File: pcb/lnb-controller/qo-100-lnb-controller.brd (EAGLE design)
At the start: 70 x 100 mm, 168 parts, among them CON1 3P-SH-SIDE, CON2 2EDG-2P-5MM, U1 EFM32PG1B100F256GM32, U10 ADP7142AUJZ-3.3, U3 DSB321SDA, U4 SI5351C-B-GM, U5 LT8650S-1, U6 AD5272-100, U7 AD5272-100, U8 MIC23155, U9 LT8636

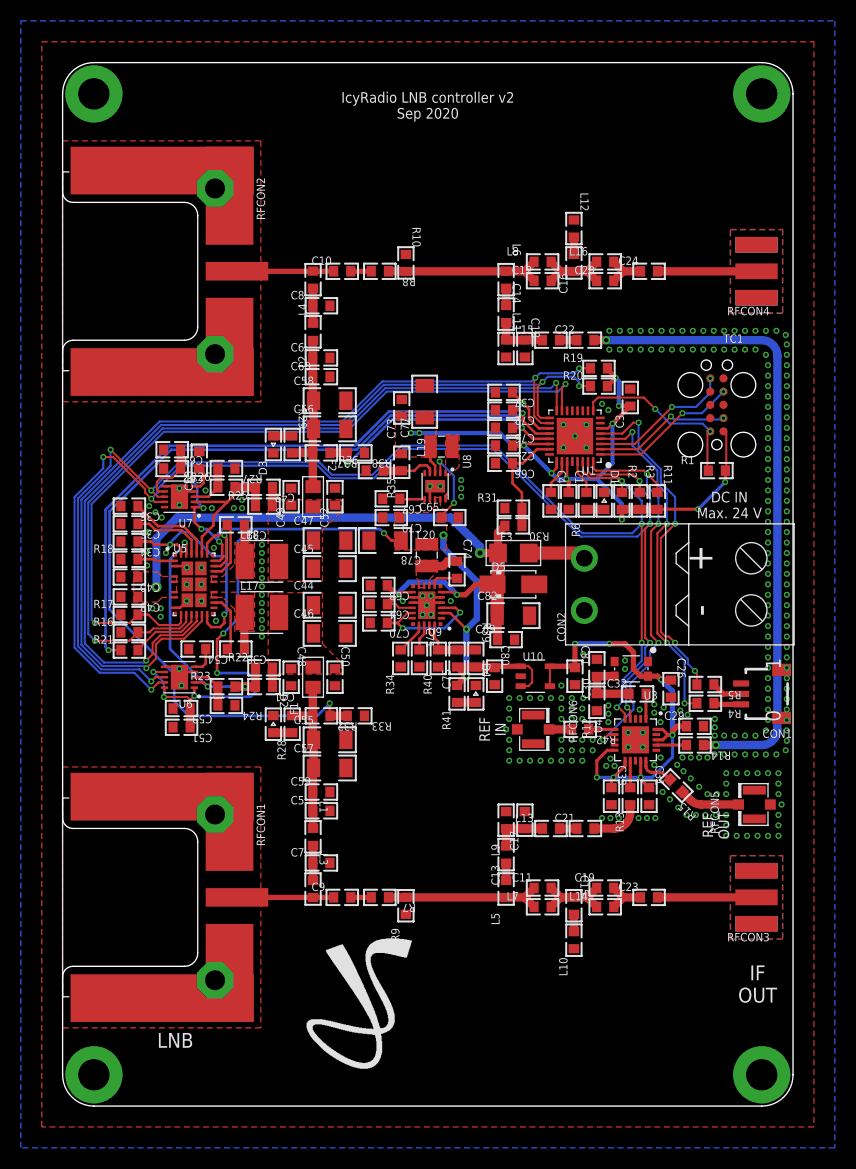
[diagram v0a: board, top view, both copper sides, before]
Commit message: Finish routing LNB Controller PCB
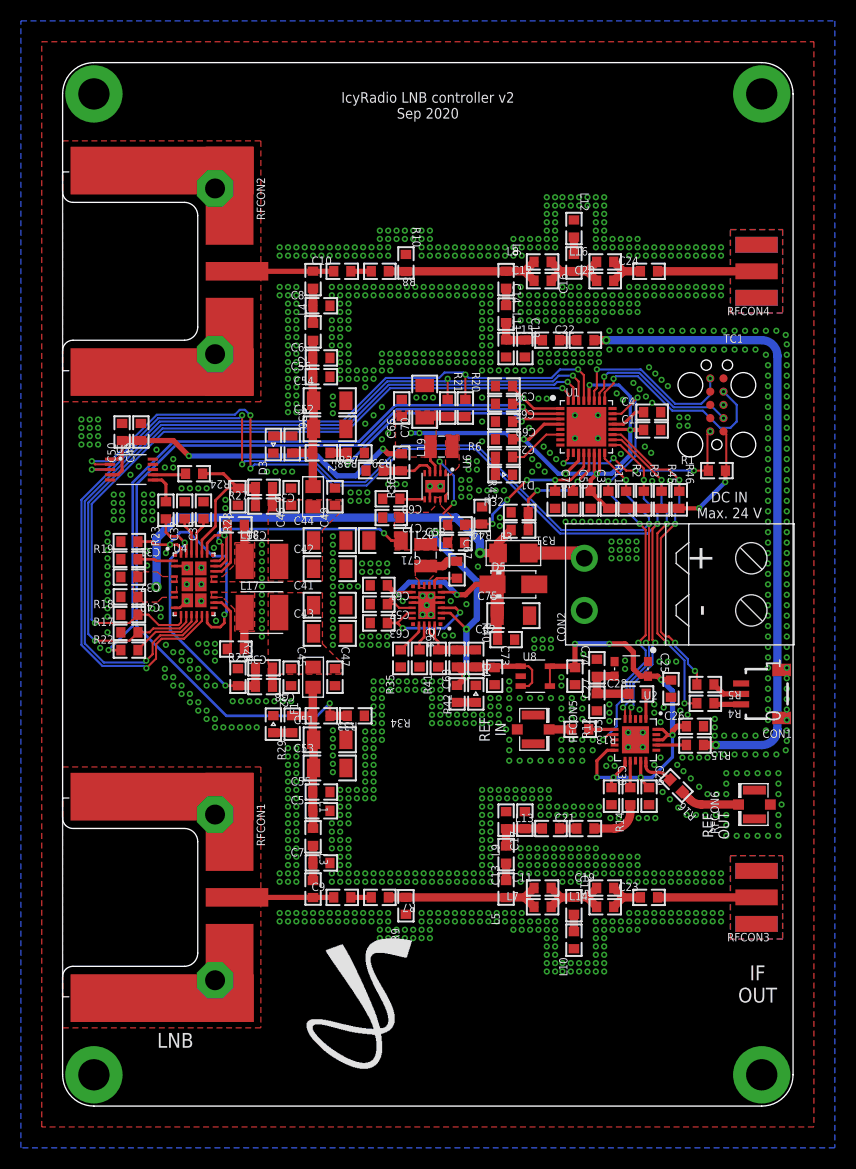
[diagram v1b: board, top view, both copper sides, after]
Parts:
- removed C77, C78: 100uF, Capacitor:CAP1206
- removed C79: 100nF, Capacitor:CAP0603
- removed C80: 1uF, Capacitor:CAP0603
- removed C81: 10uF, Capacitor:CAP0603
- removed C82: 10uF, Capacitor:CAP1206
- removed U10: ADP7142AUJZ-3.3, Analog Devices:SOT23-5
- removed U9: LT8636, Analog Devices:QFN20_ASYM_CORNER
- added C25: 100nF, Capacitor:CAP0603
- added C27, C28: 10pF, Capacitor:CAP0603
- added R43: 75K Ohms, Resistor:RES0603
- added R44: 100K Ohms, Resistor:RES0603
- added R45, R46: 1K Ohms, Resistor:RES0603
- added U2: DSB321SDA, Crystal:TCXO-3225
- C30: value 10pF -> 100nF
- C31, C62, C73: value 100nF -> 1uF
- C32: value 10pF -> 10nF
- C33: value 100nF -> 10nF
- C34, C69: value 1uF -> 470pF
- C35, C36: value 10nF -> 100nF
- C37: value 470pF -> 4.7uF
- C38, C39: value 100nF -> 4.7pF
- C40: value 4.7uF -> 1uF
- C41, C42: value 4.7pF -> 22uF; device Capacitor:CAP0603 -> Capacitor:CAP1206
- C43, C54: value 1uF -> 22uF; device Capacitor:CAP0603 -> Capacitor:CAP1206
- C45, C46, C47, C55, C56: value 22uF -> 100nF; device Capacitor:CAP1206 -> Capacitor:CAP0603
- C48, C74: value 100nF -> 10uF
- C51: value 10uF -> 22uF; device Capacitor:CAP0603 -> Capacitor:CAP1206
- C52, C53: value 100nF -> 22uF; device Capacitor:CAP0603 -> Capacitor:CAP1206
- C57, C58: value 22uF -> 4.7uF; device Capacitor:CAP1206 -> Capacitor:CAP0603
- C59, C60: value 100nF -> 470pF
- C61: value 10uF -> 1uF
- C64: value 4.7uF -> 10nF
- C65: value 4.7uF -> 470pF
- C66, C67, C72: value 470pF -> 100nF
- C68: value 1uF -> 10pF
- C70: value 1uF -> 100uF; device Capacitor:CAP0603 -> Capacitor:CAP1206
- C71: value 10nF -> 100uF; device Capacitor:CAP0603 -> Capacitor:CAP1206
- C75: value 10pF -> 10uF; device Capacitor:CAP0603 -> Capacitor:CAP1206
- R16: value 100K Ohms -> 0 Ohms
- R18: value 15K Ohms -> 100K Ohms
- R19: value 100K Ohms -> 15K Ohms
- R21: value 1K Ohms -> 100K Ohms
- R22: value 1M Ohms -> 1K Ohms
- R23: value DNP -> 191K Ohms
- R24: value 40.2K Ohms -> 191K Ohms
- R26: value DNP -> 51K Ohms
- R27: value 40.2K Ohms -> 1M Ohms
- R28: value 2.5K Ohms -> 51K Ohms
- R30: value 100K Ohms -> 2.5K Ohms
- R31: value 10K Ohms -> 100K Ohms
- R32: value 90.9K Ohms -> 10K Ohms
- R33, R38: value 12K Ohms -> 90.9K Ohms
- R34: value 41.2K Ohms -> 12K Ohms
- R35: value 309K Ohms -> 41.2K Ohms
- R36: value 71.5K Ohms -> 309K Ohms
- R37: value 90.9K Ohms -> 71.5K Ohms
- R39: value 1M Ohms -> 12K Ohms
- R4, R5: value 100 Ohms -> 0 Ohms
- R40: value 226K Ohms -> 1M Ohms
- R41: value 510 Ohms -> 226K Ohms
- R42: value 0 Ohms -> 510 Ohms
- U1: value EFM32PG1B100F256GM32 -> EFM32TG11B120F128GM32; device EFM32:QFN32_0.5P_JPG -> EFM32:QFN32_0.5P_TG
- U3: value DSB321SDA -> SI5351C-B-GM; device Crystal:TCXO-3225 -> Silicon Labs:QFN20
- U4: value SI5351C-B-GM -> LT8650S-1; device Silicon Labs:QFN20 -> Analog Devices:QFN28_ASYM_CORNER
- U5: value LT8650S-1 -> MCP4728-A2; device Analog Devices:QFN28_ASYM_CORNER -> Microchip:MSOP10
- U6: value AD5272-100 -> MIC23155; device Analog Devices:DFN10 -> Microchip:DFN10
- U7: value AD5272-100 -> LT8636; device Analog Devices:DFN10 -> Analog Devices:QFN20_ASYM_CORNER
- U8: value MIC23155 -> ADP7142AUJZ-3.3; device Microchip:DFN10 -> Analog Devices:SOT23-5
- moved C31 55.5 mm to (6.40, 54.1), turned to 180 degrees
- moved R16 54.4 mm to (58.8, 30.7), turned to 135 degrees
- moved R19 48.6 mm to (6.40, 52.4)
- moved C33 47.7 mm to (13.5, 57.1), turned to 90 degrees
- moved C32 46.8 mm to (11.7, 57.1), turned to 90 degrees
- moved U4 44.8 mm to (12.6, 50.0), turned to 0 degrees
- moved C37 40.0 mm to (6.40, 50.7)
- moved C34 38.9 mm to (42.3, 69.0)
- moved R21 38.3 mm to (36.9, 66.9), turned to 270 degrees
- moved C59 36.9 mm to (48.9, 58.1), turned to 270 degrees
- moved C62 36.0 mm to (42.5, 44.7), turned to 0 degrees
- moved C50 31.1 mm to (5.70, 64.6), turned to 90 degrees
- moved U6 30.6 mm to (35.7, 59.4), turned to 270 degrees
- moved C48 27.6 mm to (7.50, 64.6), turned to 90 degrees
- moved R32 27.2 mm to (43.8, 56.9), turned to 0 degrees
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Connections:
- removed net I2C_SCL: R3.1, U1.31, U4.4, U6.9, U7.9
- removed net I2C_SDA: R2.1, U1.30, U4.5, U6.8, U7.8
- removed net N$39: C54.1, U6.5
- removed net N$40: C63.1, U7.5
- removed net UART_RX: R4.2, U1.4
- removed net UART_TX: R5.2, U1.5
- removed net VBIAS1_FB_DIV: R23.1, R24.2, U6.3
- removed net VBIAS2_FB_DIV: R26.1, R27.2, U7.3
- new net 5V0_VSENSE: C76.1, R43.2, R44.1, U1.12
- new net I2C0_SCL: R46.1, R5.2, U1.19
- new net I2C0_SDA: R4.2, R45.1, U1.18
- new net I2C1_SCL: R3.1, U1.17, U3.4, U5.2
- new net I2C1_SDA: R2.1, U1.16, U3.5, U5.3
- new net VBIAS1_VADJ: R23.2, U5.6
- new net VBIAS2_VADJ: R24.2, U5.7
- net !REF_SYNTH_OE: now also U1.23, U3.7; no longer U1.32, U4.7
- net 3V3: now also C48.1, C50.1, C66.1, C70.1, R21.2, R36.2, R45.2, R46.2, U1.11, U1.14, U1.15, U1.20, U1.28, U1.4, U5.1, U5.4, U6.3; no longer C73.1, C77.1, R19.2, R35.2, U1.22, U1.25, U1.27, U1.6, U8.3
- net 3V3_FB: now also R36.1, R37.2, U6.4; no longer R35.1, R36.2, U8.4
- net 3V3_REF_CLEAN: now also C25.1, C30.1, C74.1, U2.4, U3.10, U3.11, U3.14, U3.18, U3.20, U8.4, U8.5; no longer C31.1, C33.1, C81.1, U10.4, U10.5, U3.4, U4.10, U4.11, U4.14, U4.18, U4.20
- net 3V3_SOFTSTART: now also C60.1, U6.6; no longer C67.1, U8.6
- net 3V3_SW: now also U6.1; no longer U8.1
- net 5V0: now also C58.1, C68.1, C71.1, C72.1, C73.1, R40.2, R42.2, R44.2, U4.22, U6.2, U6.8, U6.9, U7.2, U8.1, U8.3; no longer C51.1, C53.1, C61.1, C62.1, C65.1, C75.1, C78.1, C79.1, C80.1, R39.2, R41.2, U10.1, U10.3, U5.22, U6.1, U6.10, U6.7, U7.1, U7.7, U8.2, U8.8, U8.9, U9.2
- net 5V0_BST: now also C67.2, U7.7; no longer C74.2, U9.7
- net 5V0_FB: now also C68.2, R40.1, R41.2, U7.19, U7.20; no longer C75.2, R39.1, R40.2, U9.19, U9.20
- net 5V0_INTVCC: now also C63.1, U7.15, U7.3; no longer C70.1, U9.15, U9.3
- net 5V0_RT: now also R35.2, U7.17; no longer R34.2, U9.17
- net 5V0_SS: now also C64.1, U7.18; no longer C71.1, U9.18
- net 5V0_SW: now also C67.1, U7.10, U7.8, U7.9; no longer C74.1, U9.10, U9.8, U9.9
- net BIAS_REG_TEMP: now also C34.1, R22.1, U1.1; no longer C37.1, R21.1, U1.19
- net EXT_REF_IN: now also R13.2, RFCON5.P$3; no longer R42.2, RFCON6.P$3
- net EXT_REF_OUT: now also R16.1, RFCON6.P$3; no longer R15.1, RFCON5.P$3
- net GND: now also C25.2, C27.2, C32.2, C41.2, C42.2, C74.2, C75.2, R19.1, R26.1, R28.1, R32.1, R35.1, R37.1, R39.1, R41.1, R43.1, U2.1, U2.2, U3.21, U4.2, U4.29, U4.30, U4.31, U4.32, U4.33, U4.34, U4.35, U4.36, U4.37, U4.38, U4.7, U5.10, U6.10, U6.7, U7.12, U7.13, U7.21, U7.5, U7.M1, U7.M2, U7.M3, U7.M4, U8.2; no longer C35.2, C36.2, C67.2, C68.2, C77.2, C78.2, C79.2, C80.2, C81.2, C82.2, R16.1, R24.1, R27.1, R31.1, R33.1, R36.1, R38.1, R40.1, U10.2, U3.1, U3.2, U4.21, U5.2, U5.29, U5.30, U5.31, U5.32, U5.33, U5.34, U5.35, U5.36, U5.37, U5.38, U5.7, U6.4, U6.6, U7.10, U7.11, U7.6, U8.10, U8.11, U8.7, U9.12, U9.13, U9.21, U9.4, U9.5, U9.M1, U9.M2, U9.M3, U9.M4
- net LED: now also U1.6; no longer U1.29
- net N$1: now also R16.2, U3.15; no longer R15.2, U4.15
- net N$11: now also R29.1; no longer R28.1
- net N$149: now also R42.1; no longer R41.1
- net N$2: now also R15.2, U3.17; no longer R14.2, U4.17
- net N$23: now also R30.1; no longer R29.1
- net N$3: now also R19.2, U4.1; no longer R18.2, U5.1
- net N$36: now also C28.2, U3.1; no longer C32.2, U4.1
- net N$37: now also R13.1, U3.6; no longer R42.1, U4.6
- net N$5: now also R14.2, U3.12; no longer R13.2, U4.12
- net N$6: now also U1.21; no longer U1.26
- net N$7: now also C27.1, C28.1, U2.3; no longer C30.1, C32.1, U3.3
- net N$8: now also R22.2, U4.10; no longer R21.2, U5.10
- net REF1: now also R14.1; no longer R13.1
- net REF2: now also R15.1; no longer R14.1
- net SWCLK: now also U1.25; no longer U1.1
- net SWDIO: now also U1.26; no longer U1.2
- net SWO: now also U1.27; no longer U1.3
- net VBIAS1: now also C51.1, C53.1, R29.2, R33.2; no longer C57.1, C59.1, R28.2, R32.2
- net VBIAS1_BST: now also C35.2, U4.15; no longer C38.2, U5.15
- net VBIAS1_EN: now also R17.2, U1.31, U4.9; no longer R16.2, U1.16, U5.9
- net VBIAS1_FB: now also C38.2, R23.1, R25.1, R26.2, U4.27; no longer C41.2, R22.1, R23.2, U5.27, U6.2
- net VBIAS1_PG: now also R20.1, U1.29, U4.12; no longer R19.1, U1.18, U5.12
- net VBIAS1_SS: now also C32.1, U4.26; no longer C35.1, U5.26
- net VBIAS1_SW: now also C35.1, U4.16, U4.17; no longer C38.1, U5.16, U5.17
- net VBIAS1_UNFUSED: now also C38.1, C43.1, C45.1, C47.1, R25.2; no longer C44.1, C46.1, C48.1, C50.1, R22.2
- net VBIAS1_VSENSE: now also C65.1, R33.1, R34.2, U1.2; no longer C72.1, R32.1, R33.2, U1.20
- net VBIAS2: now also C52.1, C54.1, R30.2, R38.2; no longer C58.1, C60.1, R29.2, R37.2
- net VBIAS2_BST: now also C36.2, U4.20; no longer C39.2, U5.20
- net VBIAS2_EN: now also R18.2, U1.32, U4.8; no longer R17.2, U1.15, U5.8
- net VBIAS2_FB: now also C39.2, R24.1, R27.1, R28.2, U4.24; no longer C42.2, R25.1, R26.2, U5.24, U7.2
- net VBIAS2_PG: now also R21.1, U1.30, U4.11; no longer R20.1, U1.17, U5.11
- net VBIAS2_SS: now also C33.1, U4.25; no longer C36.1, U5.25
- net VBIAS2_SW: now also C36.1, U4.18, U4.19; no longer C39.1, U5.18, U5.19
- net VBIAS2_UNFUSED: now also C39.1, C44.1, C46.1, R27.2; no longer C45.1, C47.1, C52.1, R25.2
- net VBIAS2_VSENSE: now also C69.1, R38.1, R39.2, U1.3; no longer C76.1, R37.1, R38.2, U1.21
- net VBIAS_VCC: now also C31.1, U4.13, U4.21, U4.23, U4.28; no longer C34.1, U5.13, U5.21, U5.23, U5.28
- net VIN: now also C37.1, C57.1, C61.1, C62.1, C75.1, R31.2, U4.3, U4.4, U4.5, U4.6, U7.11, U7.14, U7.6; no longer C43.1, C64.1, C68.1, C69.1, C82.1, R30.2, U5.3, U5.4, U5.5, U5.6, U9.11, U9.14, U9.6
- net VIN_VSENSE: now also C59.1, R31.1, R32.2, U1.13; no longer C66.1, R30.1, R31.2, U1.23
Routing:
- net I2C_SCL: track 124.9 -> 0.00 mm, vias 7 -> 0
- net I2C_SDA: track 121.8 -> 0.00 mm, vias 7 -> 0
- net I2C1_SCL: track 0.00 -> 100.5 mm, vias 0 -> 7
- net I2C1_SDA: track 0.00 -> 97.7 mm, vias 0 -> 7
- net 5V0: track 114.2 -> 60.1 mm, vias 15 -> 7
- net 3V3: track 68.2 -> 113.0 mm
- net UART_RX: track 33.3 -> 0.00 mm, vias 4 -> 0
- net UART_TX: track 32.9 -> 0.00 mm, vias 4 -> 0
- net I2C0_SDA: track 0.00 -> 31.6 mm, vias 0 -> 4
- net I2C0_SCL: track 0.00 -> 31.2 mm, vias 0 -> 4
- net 5V0_VSENSE: track 0.00 -> 16.8 mm, vias 0 -> 4
- net SWCLK: track 14.3 -> 20.0 mm
- net VBIAS2_SS: track 8.35 -> 3.65 mm
- net !REF_SYNTH_OE: track 38.5 -> 43.2 mm, vias 4 -> 5
- net VBIAS2_FB_DIV: track 4.44 -> 0.00 mm
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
